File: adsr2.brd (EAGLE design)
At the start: 99.4 x 30.5 mm, 45 parts, among them IC1 LM324D, IC2 4066D, IC3 4555D, SW1_TIME TL2285, SW2_TRIG TL2285, T1 BC847, T2 BC857

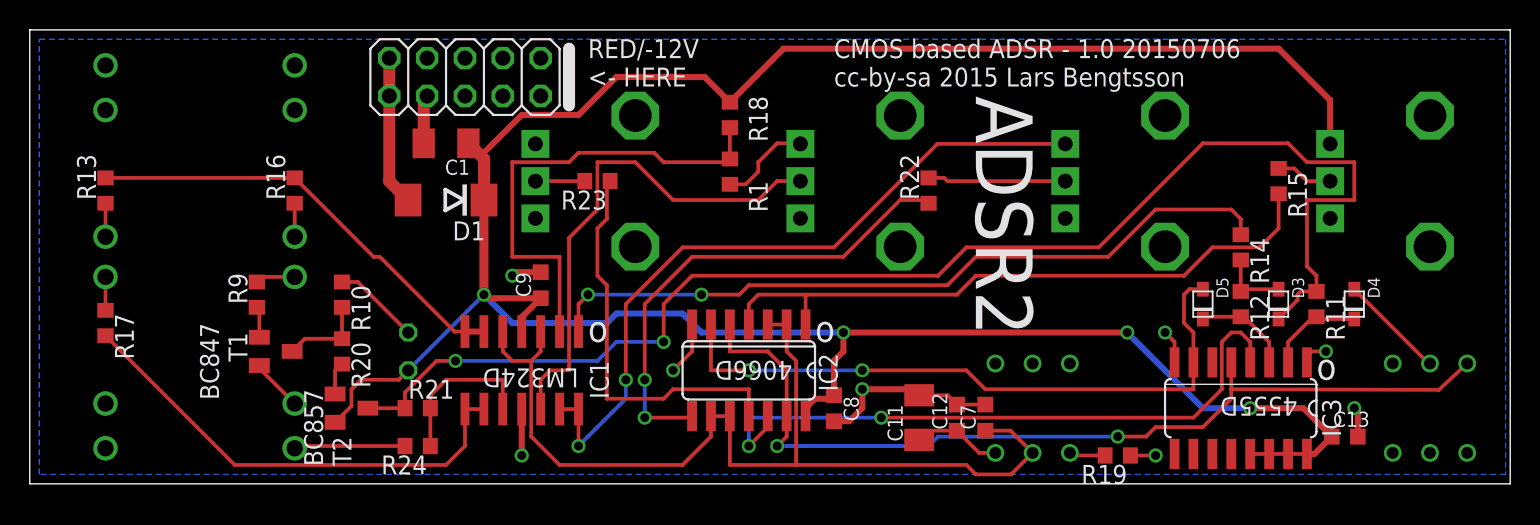
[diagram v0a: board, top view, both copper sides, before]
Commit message: Changed gate IO and outputs: Gate in, Gate thru, "Attack done" trigger out, Envelope CV Out. Removed gate thru mode selector switch. Added LED #2 for "attack done" trigger. Adjusted component labels on PCB. Added D2, prevents current leak back from diode logic surrounding IC3A to attack_done signal (affects gate output circuit if not there).
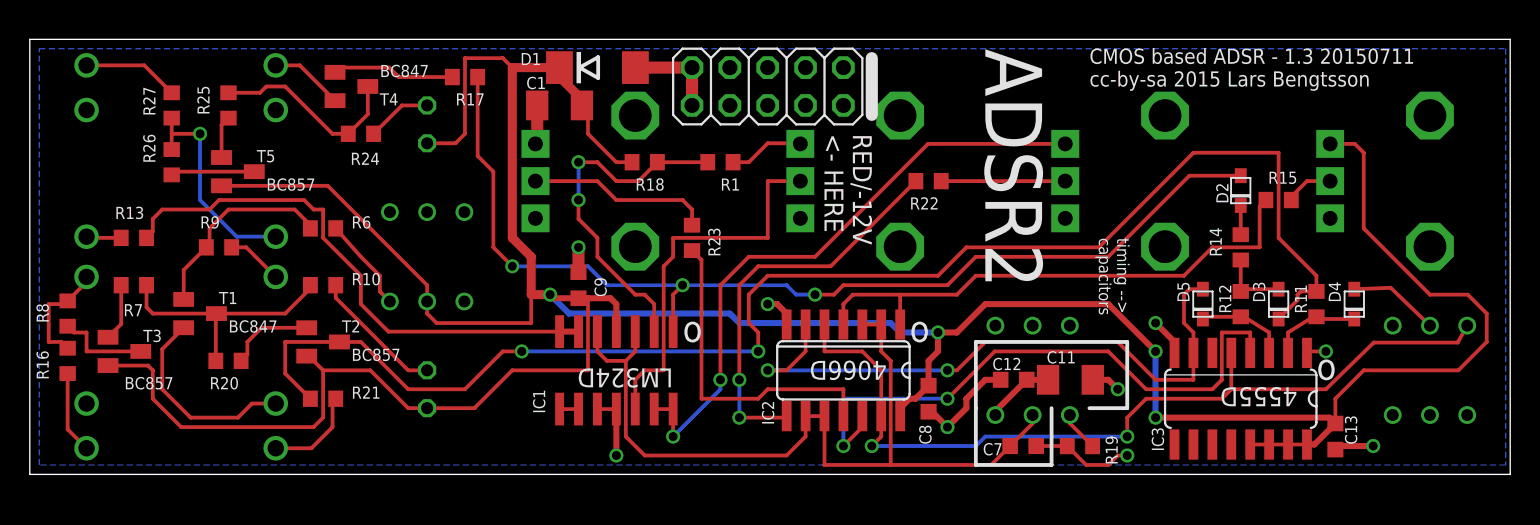
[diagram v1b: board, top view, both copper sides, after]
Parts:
- removed OUT1, OUT2: WQP-PJ301M-12_JACK, thonkiconn:WQP-PJ301M-12_JACK
- added AT_TRIG, CV_OUT: WQP-PJ301M-12_JACK, thonkiconn:WQP-PJ301M-12_JACK
- added D2: 1N4148, adafruit:SOD-323F
- added LED1: AT_TRIG_LED, led:LED3MM
- added R25, R6, R7: 100k, rcl:R0603
- added R26, R8: 4k7, rcl:R0603
- added R27: 3k3, rcl:R0603
- added SW_MANUAL: TL2285, lb_devs:TL2285_PCB
- added T3, T5: BC857, transistor:SOT23-BEC
- added T4: BC847, transistor:SOT23
- R16: value 1k -> 3k3
- R17: value 1k -> 100k
- R21: value 4k7 -> 10k
- R24: value 3k3 -> 10k
- moved R17 29.2 mm to (29.2, 37.5), turned to 0 degrees
- moved R24 21.3 mm to (22.2, 33.7)
- moved JP1 20.3 mm to (49.5, 36.8)
- moved R16 19.1 mm to (2.54, 18.4), turned to 270 degrees
- moved D1 13.5 mm to (38.1, 38.1), turned to 0 degrees
- moved C11 10.5 mm to (69.8, 17.1), turned to 0 degrees
- moved C1 8.03 mm to (35.6, 35.6)
- moved R20 7.65 mm to (13.3, 18.4), turned to 0 degrees
- moved R23 7.41 mm to (44.5, 26.7), turned to 90 degrees
- moved R18 6.54 mm to (41.3, 31.8), turned to 0 degrees
- moved C8 6.38 mm to (60.3, 15.9)
- moved R21 6.38 mm to (19.7, 15.9)
- moved IC2 6.35 mm to (54.6, 17.8)
- moved IC1 6.35 mm to (39.4, 17.8)
- moved T1 5.68 mm to (11.4, 21.6)
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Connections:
- removed net N$14: GATE_THRU.P$1, R17.1
- new net N$29: D2.C, R14.1
- new net N$30: R24.2, R25.1, T4.3
- new net N$31: LED1.K, R24.1
- new net N$33: R25.2, T5.B
- new net N$34: R26.1, T5.C
- new net N$35: AT_TRIG.P$1, R26.2, R27.1
- new net N$4: R6.2, SW_MANUAL.4
- new net N$8: R7.2, T3.B
- new net N$9: R8.1, T3.C
- net +12V: now also LED1.A, SW_MANUAL.5, T3.E, T5.E
- net ATTACK_DONE: now also D2.A, R17.2; no longer R14.1
- net GATE_IN: now also R7.1
- net GND: now also AT_TRIG.P$3, CV_OUT.P$3, IC1.10, R16.2, R21.2, R27.2, T4.2; no longer OUT1.P$3, OUT2.P$3, R24.2
- net N$11: now also CV_OUT.P$1; no longer OUT2.P$1
- net N$12: no longer R16.2
- net N$13: now also GATE_THRU.P$1, R16.1, R8.2; no longer IC1.10, R21.2, R24.1
- net N$19: now also R17.1, T4.1; no longer OUT1.P$1, R16.1
- net N$21: now also R6.1
- net N$24: no longer R17.2
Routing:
- net +12V: track 171.9 -> 228.8 mm
- net N$24: track 32.0 -> 1.27 mm
- net GND: track 43.7 -> 70.7 mm, vias 8 -> 9
- net ATTACK_DONE: track 50.2 -> 70.0 mm, vias 2 -> 3
- net N$35: track 0.00 -> 14.6 mm, vias 0 -> 1
- net N$30: track 0.00 -> 13.2 mm
- net N$21: track 2.08 -> 13.4 mm
- net GATE_IN: track 5.81 -> 16.8 mm
- net ENV_CAP: track 66.4 -> 56.6 mm
- net N$23: track 3.31 -> 12.4 mm
- net SUST_LEVEL: track 34.1 -> 25.6 mm
- net ATTACK_REF: track 31.9 -> 23.6 mm, vias 0 -> 2
- net N$10: track 43.4 -> 36.2 mm
- net N$7: track 48.5 -> 41.7 mm
- net N$12: track 29.7 -> 36.4 mm
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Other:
- board size 99.4 x 30.5 mm -> 99.4 x 29.2 mm
- board text added: "CMOS based ADSR - 1.3 20150711 cc-by-sa 2015 Lars Bengtsson"
- board text added: "timing --> capacitors"
- board text removed: "CMOS based ADSR - 1.0 20150706 cc-by-sa 2015 Lars Bengtsson"

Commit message: Minor routing fixes & components moved.
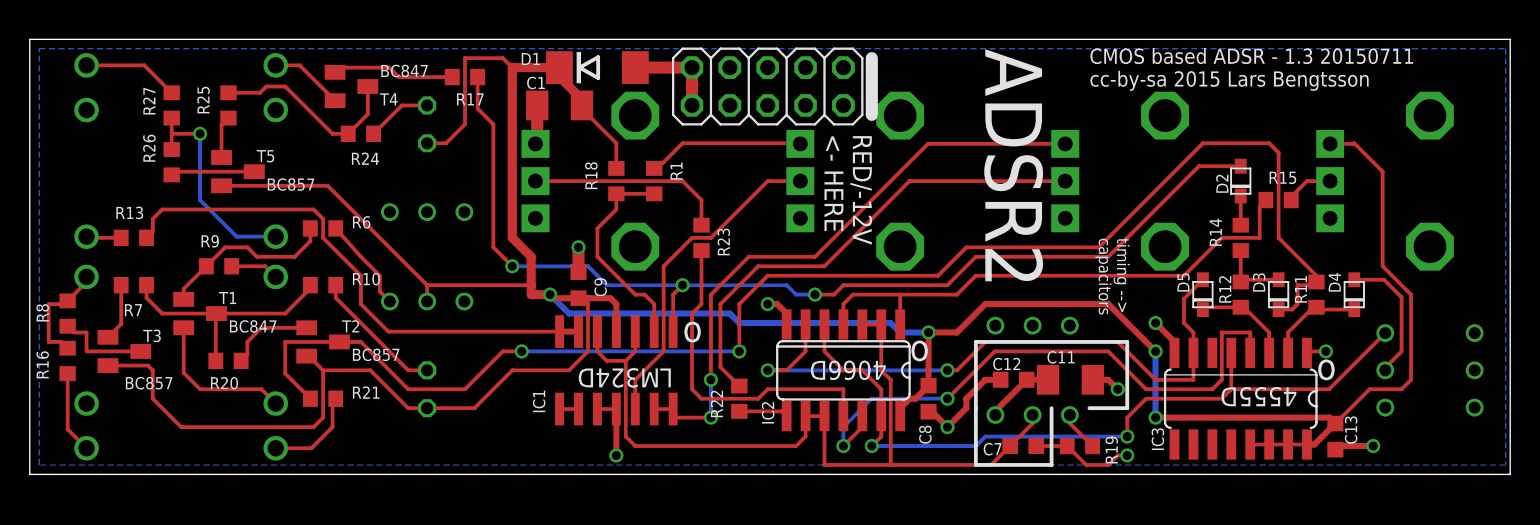
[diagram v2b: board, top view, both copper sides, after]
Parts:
- SW1_TIME, SW2_TRIG: value TL2285 -> TL2285 L
- SW_MANUAL: value TL2285 -> TL2285 Mom.
- moved R22 19.4 mm to (47.6, 15.9), turned to 90 degrees
- moved R1 4.62 mm to (41.9, 30.5), turned to 90 degrees
- moved R18 2.29 mm to (39.4, 30.5), turned to 270 degrees
- moved R9 1.27 mm to (12.7, 24.8)
- moved D2 0.64 mm to (81.3, 30.5)
- moved R14 0.64 mm to (81.3, 26.7)
- moved D3 0.63 mm to (83.8, 22.9)
- moved D4 0.63 mm to (88.9, 22.9)
- moved D5 0.63 mm to (78.7, 22.9)
- moved R11 0.63 mm to (86.4, 22.9)
- moved R12 0.63 mm to (81.3, 22.9)
- moved R23 0.63 mm to (45.1, 26.7)
- turned SW2_TRIG to 90 degrees
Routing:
- net N$15: track 8.33 -> 32.6 mm
- net N$6: track 26.9 -> 3.31 mm, vias 2 -> 0
- net +12V: track 228.8 -> 215.7 mm
- net ATTACK_REF: track 23.6 -> 14.3 mm, vias 2 -> 0
- net ATTACK: track 58.1 -> 51.5 mm
- net N$26: track 5.06 -> 10.5 mm
- net SUST_LEVEL: track 25.6 -> 21.9 mm
- net GND: track 70.7 -> 67.3 mm
- net N$27: track 6.11 -> 9.02 mm
- net N$21: track 13.4 -> 11.9 mm
- net RELEASE: track 40.2 -> 39.1 mm
- net N$7: track 41.7 -> 40.6 mm
- net N$23: track 12.4 -> 13.4 mm
- net N$12: track 36.4 -> 35.5 mm
- net GATE: track 96.3 -> 95.5 mm
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
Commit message: Some more routing fixes near jacks. Updated date stamp in PCB text labels.
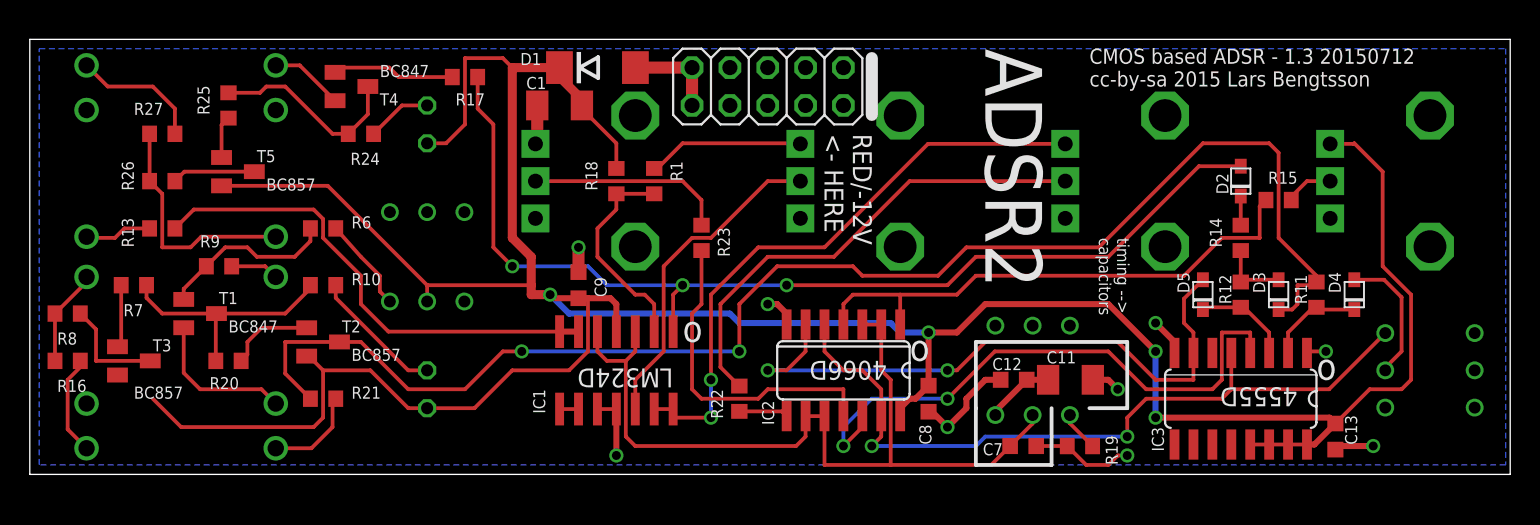
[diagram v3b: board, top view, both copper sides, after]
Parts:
- moved R27 2.01 mm to (8.89, 33.7), turned to 0 degrees
- moved R13 2.01 mm to (8.89, 27.3)
- moved R26 1.42 mm to (8.89, 30.5), turned to 180 degrees
- moved T3 0.90 mm to (6.99, 18.4)
- turned R16 to 0 degrees
- turned R8 to 180 degrees
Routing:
- net +12V: track 215.7 -> 210.6 mm
- net GND: track 67.3 -> 70.8 mm
- net N$12: track 35.5 -> 32.9 mm
- net N$11: track 2.36 -> 4.53 mm
- net N$35: track 14.6 -> 15.9 mm, vias 1 -> 0
- net N$13: track 7.48 -> 6.51 mm
- net N$9: track 6.35 -> 7.25 mm
- net GATE: track 95.5 -> 96.0 mm
- net ATTACK_DONE: track 70.3 -> 69.8 mm
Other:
- board text added: "CMOS based ADSR - 1.3 20150712 cc-by-sa 2015 Lars Bengtsson"
- board text removed: "CMOS based ADSR - 1.3 20150711 cc-by-sa 2015 Lars Bengtsson"
